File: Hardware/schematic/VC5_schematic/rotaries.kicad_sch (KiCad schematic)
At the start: 39 parts, among them U6 MCP23017

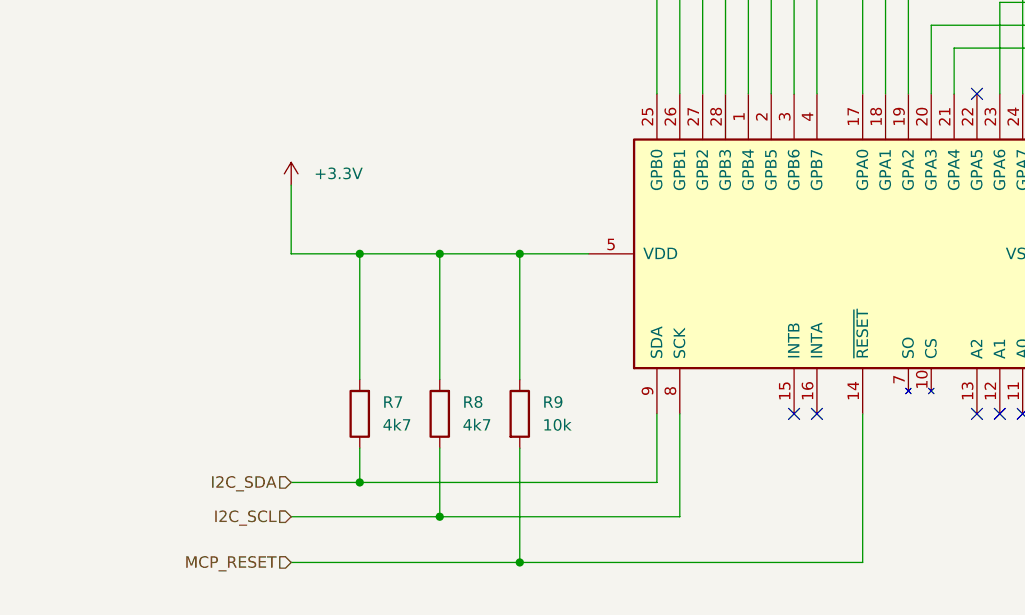
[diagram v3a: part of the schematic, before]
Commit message: fixed missing interrupt line
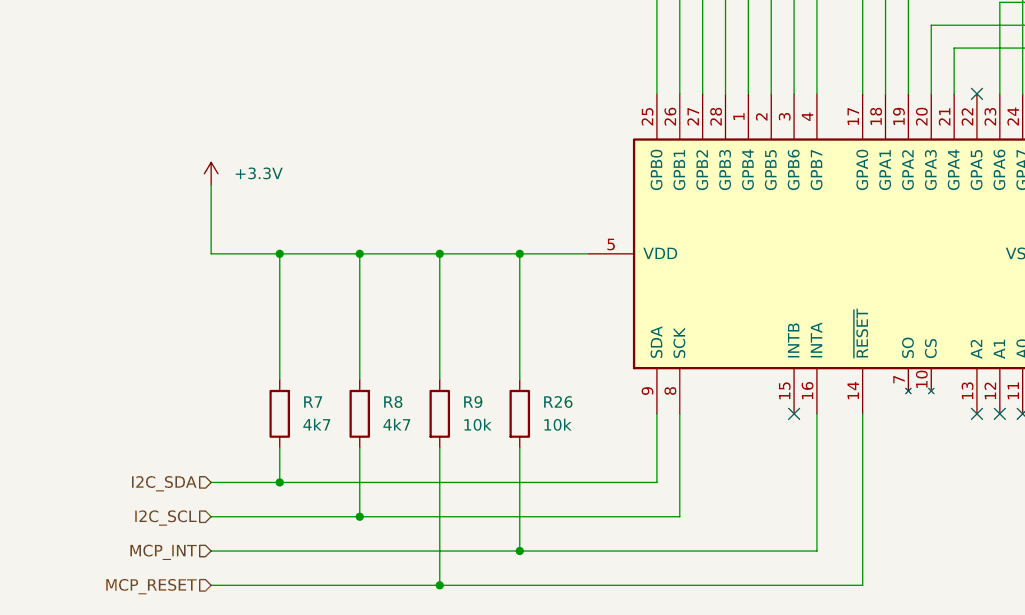
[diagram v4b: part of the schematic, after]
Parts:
- added R26: 10k, Resistor_THT:R_Axial_DIN0204_L3.6mm_D1.6mm_P7.62mm_Horizontal, symbol Device:R
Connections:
- net +3.3V: now also R26.1
- net MCP_INT: now reaches U6.16 (INTA)
- net MCP_INT: now also R26.2
- no-connect marks 6 -> 5
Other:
- moved on the sheet: R7, R8, R9

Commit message: final version of the PCB
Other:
- moved on the sheet: R26, R9
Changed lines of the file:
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@@
 	)
 	(junction
-		(at 62.23 193.04)
+		(at 71.12 193.04)
 		(diameter 0)
 		(color 0 0 0 0)
 	)
 	(junction
-		(at 62.23 156.21)
+		(at 71.12 156.21)
 		(diameter 0)
 		(color 0 0 0 0)
@@
 	)
 	(junction
-		(at 71.12 189.23)
+		(at 62.23 189.23)
 		(diameter 0)
 		(color 0 0 0 0)
 	)
 	(junction
-		(at 257.81 91.44)
+		(at 62.23 156.21)
 		(diameter 0)
 		(color 0 0 0 0)
 	)
 	(junction
-		(at 71.12 156.21)
+		(at 257.81 91.44)
 		(diameter 0)
 		(color 0 0 0 0)
@@
 	(wire
 		(pts
-			(xy 71.12 177.8) (xy 71.12 189.23)
-		)
-		(stroke
-			(width 0)
-			(type default)
-		)
-	)
-	(wire
-		(pts
 			(xy 187.96 39.37) (xy 187.96 53.34)
 		)
@@
 	(wire
 		(pts
-			(xy 62.23 177.8) (xy 62.23 193.04)
+			(xy 71.12 177.8) (xy 71.12 193.04)
 		)
 		(stroke
@@
 	(wire
 		(pts
+			(xy 62.23 177.8) (xy 62.23 189.23)
+		)
+		(stroke
+			(width 0)
+			(type default)
+		)
+	)
+	(wire
+		(pts
 			(xy 99.06 113.03) (xy 99.06 138.43)
 		)
@@
 	(wire
 		(pts
+			(xy 62.23 189.23) (xy 104.14 189.23)
+		)
+		(stroke
+			(width 0)
+			(type default)
+		)
+	)
+	(wire
+		(pts
 			(xy 29.21 39.37) (xy 26.67 39.37)
 		)
@@
 	(wire
 		(pts
-			(xy 62.23 156.21) (xy 62.23 170.18)
+			(xy 71.12 156.21) (xy 71.12 170.18)
 		)
 		(stroke
@@
 	(wire
 		(pts
-			(xy 36.83 193.04) (xy 62.23 193.04)
+			(xy 62.23 156.21) (xy 71.12 156.21)
+		)
+		(stroke
+			(width 0)
+			(type default)
+		)
+	)
+	(wire
+		(pts
+			(xy 36.83 193.04) (xy 71.12 193.04)
 		)
 		(stroke
@@
 	(wire
 		(pts
-			(xy 62.23 193.04) (xy 109.22 193.04)
-		)
-		(stroke
-			(width 0)
-			(type default)
-		)
-	)
-	(wire
-		(pts
 			(xy 204.47 19.05) (xy 217.17 19.05)
 		)
@@
 	(wire
 		(pts
-			(xy 71.12 156.21) (xy 78.74 156.21)
-		)
-		(stroke
-			(width 0)
-			(type default)
-		)
-	)
-	(wire
-		(pts
 			(xy 116.84 130.81) (xy 116.84 138.43)
 		)
@@
 	(wire
 		(pts
-			(xy 36.83 189.23) (xy 71.12 189.23)
+			(xy 36.83 189.23) (xy 62.23 189.23)
 		)
 		(stroke
@@
 	(wire
 		(pts
-			(xy 109.22 41.91) (xy 109.22 110.49)
+			(xy 71.12 193.04) (xy 109.22 193.04)
 		)
 		(stroke
@@
 	(wire
 		(pts
-			(xy 133.35 31.75) (xy 133.35 39.37)
+			(xy 109.22 41.91) (xy 109.22 110.49)
 		)
 		(stroke
@@
 	(wire
 		(pts
-			(xy 71.12 156.21) (xy 71.12 170.18)
+			(xy 133.35 31.75) (xy 133.35 39.37)
 		)
 		(stroke
@@
 	(wire
 		(pts
+			(xy 62.23 156.21) (xy 62.23 170.18)
+		)
+		(stroke
+			(width 0)
+			(type default)
+		)
+	)
+	(wire
+		(pts
 			(xy 83.82 41.91) (xy 77.47 41.91)
 		)
@@
 	(wire
 		(pts
-			(xy 62.23 156.21) (xy 71.12 156.21)
-		)
-		(stroke
-			(width 0)
-			(type default)
-		)
-	)
-	(wire
-		(pts
 			(xy 190.5 44.45) (xy 190.5 73.66)
 		)
@@
 	(wire
 		(pts
-			(xy 71.12 189.23) (xy 104.14 189.23)
-		)
-		(stroke
-			(width 0)
-			(type default)
-		)
-	)
-	(wire
-		(pts
 			(xy 190.5 83.82) (xy 190.5 133.35)
 		)
@@
 	(wire
 		(pts
+			(xy 71.12 156.21) (xy 78.74 156.21)
+		)
+		(stroke
+			(width 0)
+			(type default)
+		)
+	)
+	(wire
+		(pts
 			(xy 26.67 60.96) (xy 26.67 63.5)
 		)
@@
 	(symbol
 		(lib_id "Device:R")
-		(at 71.12 173.99 0)
+		(at 62.23 173.99 0)
 		(unit 1)
 		(exclude_from_sim no)
@@
 		(fields_autoplaced yes)
 		(property "Reference" "R26"
-			(at 73.66 172.7199 0)
+			(at 64.77 172.7199 0)
 			(effects
 				(font
@@
 		)
 		(property "Value" "10k"
-			(at 73.66 175.2599 0)
+			(at 64.77 175.2599 0)
 			(effects
 				(font
@@
 		)
 		(property "Footprint" "Resistor_THT:R_Axial_DIN0204_L3.6mm_D1.6mm_P7.62mm_Horizontal"
-			(at 69.342 173.99 90)
+			(at 60.452 173.99 90)
 			(effects
 				(font
@@
 		)
 		(property "Datasheet" "~"
-			(at 71.12 173.99 0)
+			(at 62.23 173.99 0)
 			(effects
 				(font
@@
 		)
 		(property "Description" "Resistor"
-			(at 71.12 173.99 0)
+			(at 62.23 173.99 0)
 			(effects
 				(font
@@
 	(symbol
 		(lib_id "Device:R")
-		(at 62.23 173.99 0)
+		(at 71.12 173.99 0)
 		(unit 1)
 		(exclude_from_sim no)
@@
 		(fields_autoplaced yes)
 		(property "Reference" "R9"
-			(at 64.77 172.7199 0)
+			(at 73.66 172.7199 0)
 			(effects
 				(font
@@
 		)
 		(property "Value" "10k"
-			(at 64.77 175.2599 0)
+			(at 73.66 175.2599 0)
 			(effects
 				(font
@@
 		)
 		(property "Footprint" "Resistor_THT:R_Axial_DIN0204_L3.6mm_D1.6mm_P7.62mm_Horizontal"
-			(at 60.452 173.99 90)
+			(at 69.342 173.99 90)
 			(effects
 				(font
@@
 		)
 		(property "Datasheet" "~"
-			(at 62.23 173.99 0)
+			(at 71.12 173.99 0)
 			(effects
 				(font
@@
 		)
 		(property "Description" "Resistor"
-			(at 62.23 173.99 0)
+			(at 71.12 173.99 0)
 			(effects
 				(font
